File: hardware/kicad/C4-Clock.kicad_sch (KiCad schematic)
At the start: 39 parts, among them J1 Keypad, J2 Battery, J3 LCD1602, J4 Boost Module, J5 ICSP, K1 FINDER-36.11-5V, Q1 S9014, Q2 S9014, Q3 S9014, SW1 SW_SPST, SW2 SW_SPST, U1 ATmega328P-P, U2 AMS1117-5.0, U3 PCF8574A, U4 DS1302+, Y1 16MHz, Y2 32.768kHz

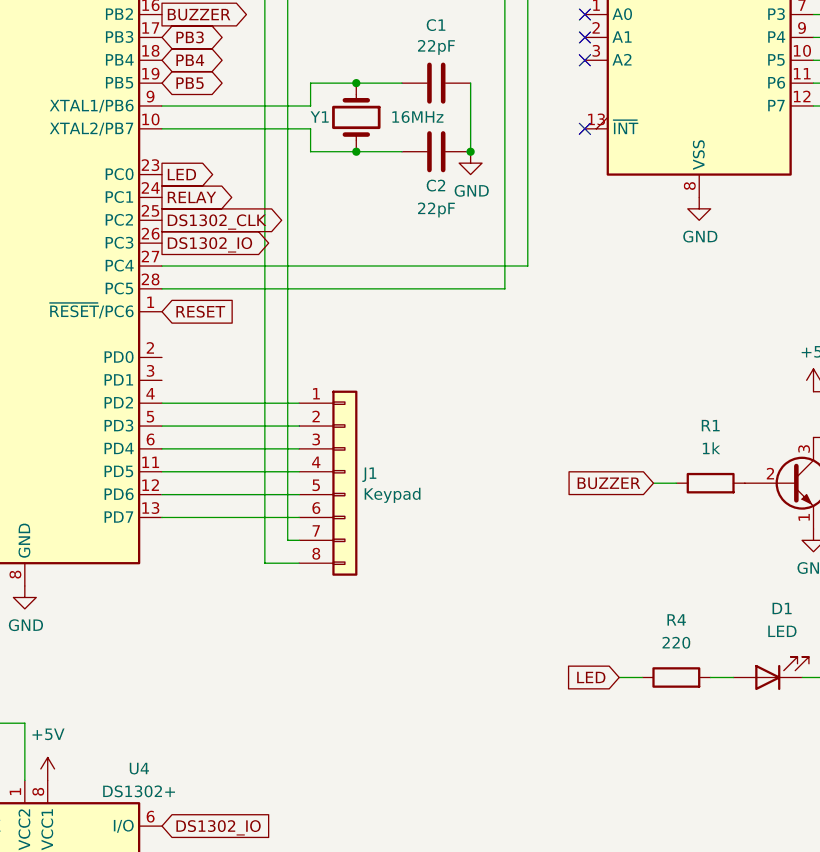
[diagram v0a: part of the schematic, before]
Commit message: kicad: Remove unused pin A0
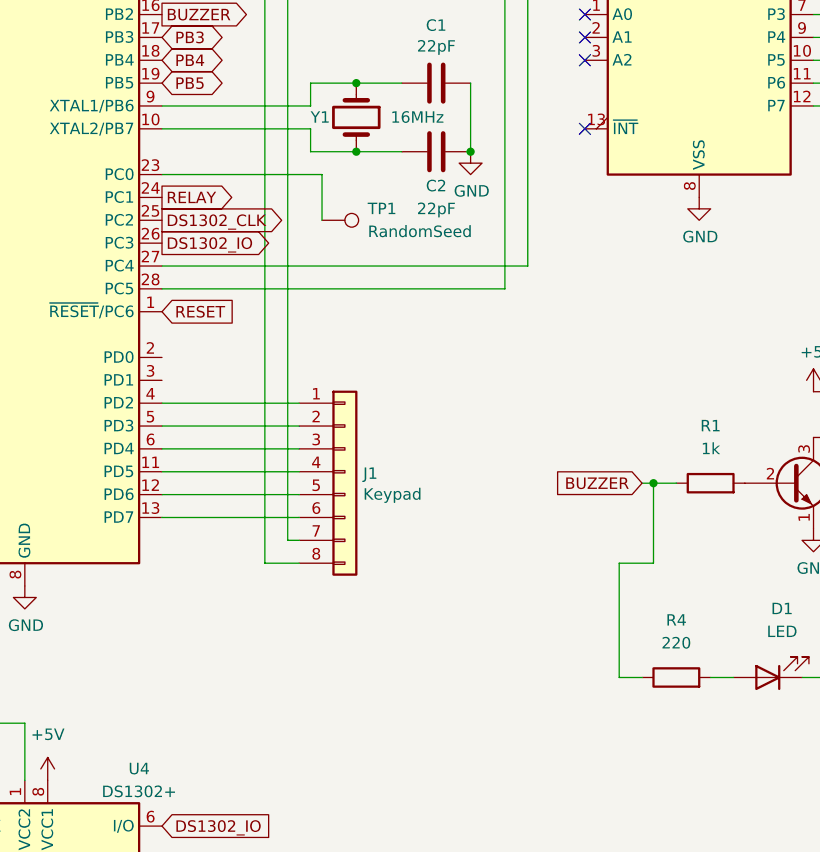
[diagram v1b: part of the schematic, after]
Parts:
- added TP1: RandomSeed, TestPoint:TestPoint_Pad_D1.0mm, symbol Connector:TestPoint
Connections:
- net BUZZER: now also R4.1
- net LED: no longer names the net of U1.23 (PC0)
- net LED: now also TP1.1; no longer R4.1
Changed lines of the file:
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@@
   (junction (at 228.6 67.31) (diameter 0) (color 0 0 0 0)
+  )
+  (junction (at 139.7 113.03) (diameter 0) (color 0 0 0 0)
   )
   (junction (at 119.38 76.2) (diameter 0) (color 0 0 0 0)
@@
     (stroke (width 0) (type default) (color 0 0 0 0))
   )
+  (wire (pts (xy 85.09 78.74) (xy 102.87 78.74))
+    (stroke (width 0) (type default) (color 0 0 0 0))
+  )
   (wire (pts (xy 106.68 68.58) (xy 111.76 68.58))
     (stroke (width 0) (type default) (color 0 0 0 0))
@@
     (stroke (width 0) (type default) (color 0 0 0 0))
   )
+  (wire (pts (xy 135.89 121.92) (xy 135.89 134.62))
+    (stroke (width 0) (type default) (color 0 0 0 0))
+  )
   (wire (pts (xy 220.98 135.89) (xy 213.36 135.89))
     (stroke (width 0) (type default) (color 0 0 0 0))
@@
     (stroke (width 0) (type default) (color 0 0 0 0))
   )
+  (wire (pts (xy 139.7 121.92) (xy 135.89 121.92))
+    (stroke (width 0) (type default) (color 0 0 0 0))
+  )
   (wire (pts (xy 71.12 44.45) (xy 69.85 44.45))
     (stroke (width 0) (type default) (color 0 0 0 0))
@@
     (stroke (width 0) (type default) (color 0 0 0 0))
   )
+  (wire (pts (xy 138.43 113.03) (xy 139.7 113.03))
+    (stroke (width 0) (type default) (color 0 0 0 0))
+  )
+  (wire (pts (xy 190.5 135.89) (xy 205.74 135.89))
+    (stroke (width 0) (type default) (color 0 0 0 0))
+  )
+  (wire (pts (xy 236.22 114.3) (xy 236.22 116.84))
+    (stroke (width 0) (type default) (color 0 0 0 0))
+  )
+  (wire (pts (xy 228.6 62.23) (xy 228.6 67.31))
+    (stroke (width 0) (type default) (color 0 0 0 0))
+  )
+  (wire (pts (xy 212.09 67.31) (xy 212.09 72.39))
+    (stroke (width 0) (type default) (color 0 0 0 0))
+  )
+  (wire (pts (xy 96.52 121.92) (xy 96.52 58.42))
+    (stroke (width 0) (type default) (color 0 0 0 0))
+  )
+  (wire (pts (xy 220.98 114.3) (xy 220.98 116.84))
+    (stroke (width 0) (type default) (color 0 0 0 0))
+  )
+  (wire (pts (xy 102.87 78.74) (xy 102.87 83.82))
+    (stroke (width 0) (type default) (color 0 0 0 0))
+  )
   (wire (pts (xy 139.7 113.03) (xy 142.24 113.03))
     (stroke (width 0) (type default) (color 0 0 0 0))
   )
-  (wire (pts (xy 190.5 135.89) (xy 205.74 135.89))
-    (stroke (width 0) (type default) (color 0 0 0 0))
-  )
-  (wire (pts (xy 236.22 114.3) (xy 236.22 116.84))
-    (stroke (width 0) (type default) (color 0 0 0 0))
-  )
-  (wire (pts (xy 228.6 62.23) (xy 228.6 67.31))
-    (stroke (width 0) (type default) (color 0 0 0 0))
-  )
-  (wire (pts (xy 212.09 67.31) (xy 212.09 72.39))
-    (stroke (width 0) (type default) (color 0 0 0 0))
-  )
-  (wire (pts (xy 96.52 121.92) (xy 96.52 58.42))
-    (stroke (width 0) (type default) (color 0 0 0 0))
-  )
-  (wire (pts (xy 220.98 114.3) (xy 220.98 116.84))
-    (stroke (width 0) (type default) (color 0 0 0 0))
-  )
   (wire (pts (xy 96.52 58.42) (xy 85.09 58.42))
     (stroke (width 0) (type default) (color 0 0 0 0))
@@
   )
   (wire (pts (xy 85.09 116.84) (xy 100.33 116.84))
+    (stroke (width 0) (type default) (color 0 0 0 0))
+  )
+  (wire (pts (xy 139.7 113.03) (xy 139.7 121.92))
     (stroke (width 0) (type default) (color 0 0 0 0))
   )
@@
   (text "En" (at 200.66 50.8 0)
     (effects (font (size 1.27 1.27)) (justify left bottom))
-  )
-  (global_label "LED" (shape input) (at 135.89 134.62 180) (fields_autoplaced)
-    (effects (font (size 1.27 1.27)) (justify right))
-    (property "Intersheet References" "${INTERSHEET_REFS}" (id 0) (at 130.1187 134.5406 0)
-      (effects (font (size 1.27 1.27)) (justify right) hide)
-    )
   )
   (global_label "PB5" (shape bidirectional) (at 30.48 34.29 180) (fields_autoplaced)
@@
     )
   )
-  (global_label "BUZZER" (shape input) (at 139.7 113.03 180) (fields_autoplaced)
+  (global_label "BUZZER" (shape input) (at 138.43 113.03 180) (fields_autoplaced)
     (effects (font (size 1.27 1.27)) (justify right))
-    (property "Intersheet References" "${INTERSHEET_REFS}" (id 0) (at -10.16 0 0)
+    (property "Intersheet References" "${INTERSHEET_REFS}" (id 0) (at -11.43 0 0)
       (effects (font (size 1.27 1.27)) hide)
     )
@@
     (property "Intersheet References" "${INTERSHEET_REFS}" (id 0) (at 22.4106 36.7506 0)
       (effects (font (size 1.27 1.27)) (justify right) hide)
-    )
-  )
-  (global_label "LED" (shape output) (at 85.09 78.74 0) (fields_autoplaced)
-    (effects (font (size 1.27 1.27)) (justify left))
-    (property "Intersheet References" "${INTERSHEET_REFS}" (id 0) (at 90.8613 78.6606 0)
-      (effects (font (size 1.27 1.27)) (justify left) hide)
     )
   )
@@
     (pin "2")
   )
+  (symbol (lib_id "Connector:TestPoint") (at 102.87 83.82 270) (unit 1)
+    (in_bom yes) (on_board yes) (fields_autoplaced)
+    (property "Reference" "TP1" (id 0) (at 107.95 82.5499 90)
+      (effects (font (size 1.27 1.27)) (justify left))
+    )
+    (property "Value" "RandomSeed" (id 1) (at 107.95 85.0899 90)
+      (effects (font (size 1.27 1.27)) (justify left))
+    )
+    (property "Footprint" "TestPoint:TestPoint_Pad_D1.0mm" (id 2) (at 102.87 88.9 0)
+      (effects (font (size 1.27 1.27)) hide)
+    )
+    (property "Datasheet" "~" (id 3) (at 102.87 88.9 0)
+      (effects (font (size 1.27 1.27)) hide)
+    )
+    (pin "1")
+  )
   (symbol (lib_id "Mechanical:MountingHole_Pad") (at 205.74 111.76 0) (unit 1)
     (in_bom yes) (on_board yes) (fields_autoplaced)
@@
       (reference "SW2") (unit 1) (value "SW_SPST") (footprint "Button_Switch_THT:SW_Push_2P2T_Toggle_CK_PVA2xxH1xxxxxxV2")
     )
+    (path "/49835dfc-d2d1-4b42-936d-27332303c393"
+      (reference "TP1") (unit 1) (value "RandomSeed") (footprint "TestPoint:TestPoint_Pad_D1.0mm")
+    )
     (path "/20f5379c-7d1a-4093-921b-363ef364bc02"

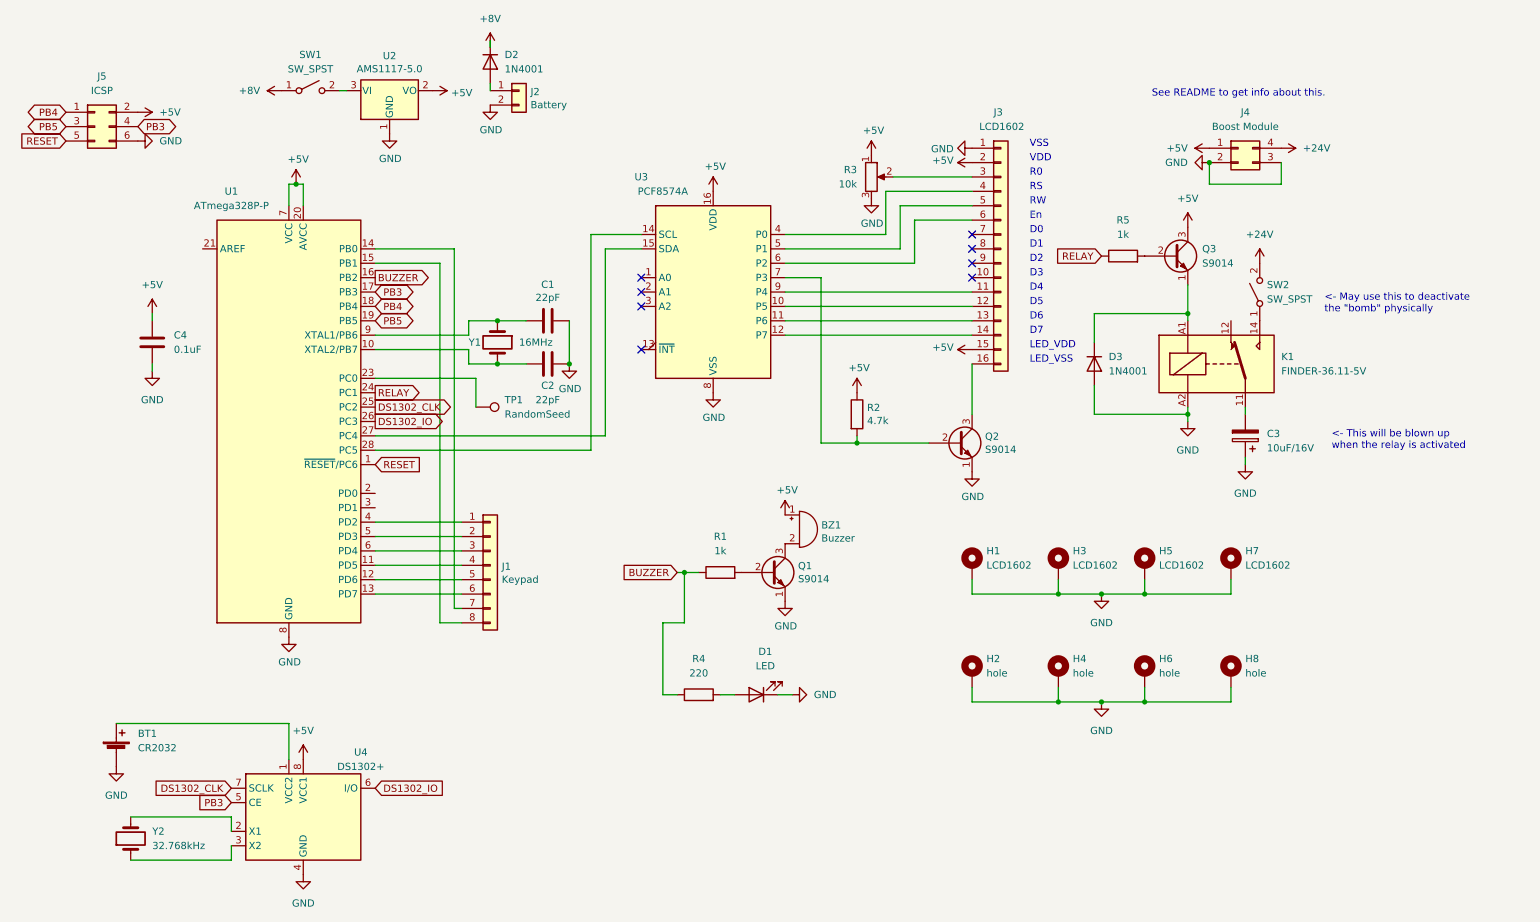
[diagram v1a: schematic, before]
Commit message: kicad: removed DS1302 and atmega
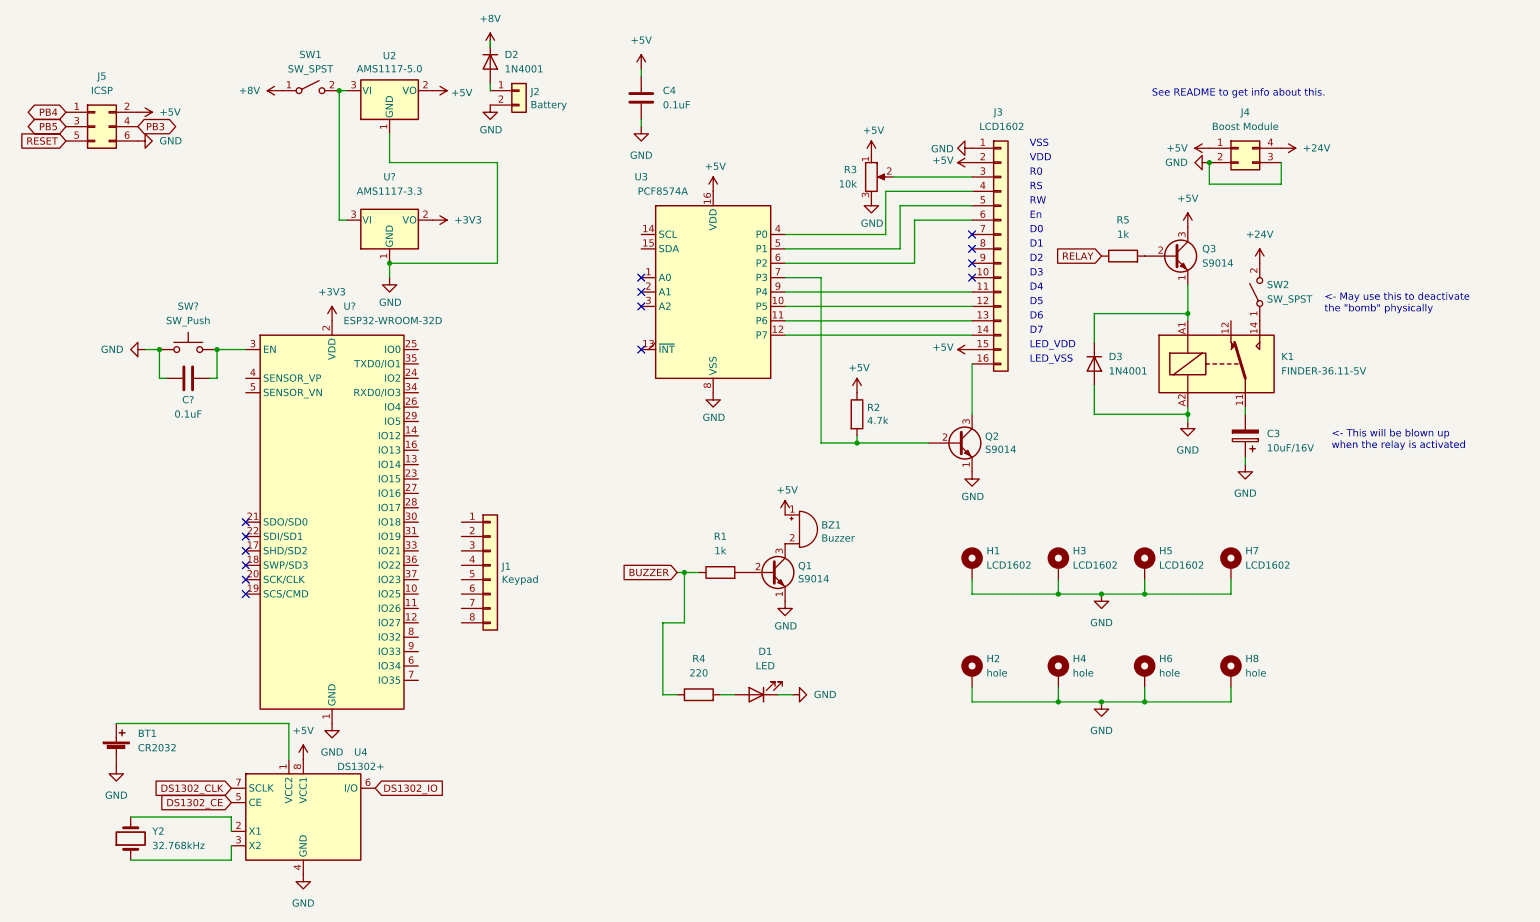
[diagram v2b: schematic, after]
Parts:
- removed C1, C2: 22pF, Capacitor_THT:C_Disc_D4.3mm_W1.9mm_P5.00mm, symbol Device:C
- removed TP1: RandomSeed, TestPoint:TestPoint_Pad_D1.0mm, symbol Connector:TestPoint
- removed U1: ATmega328P-P, Package_DIP:DIP-28_W7.62mm_Socket, symbol MCU_Microchip_ATmega:ATmega328P-P
- removed Y1: 16MHz, Crystal:Crystal_HC49-4H_Vertical, symbol Device:Crystal
- added C?: 0.1uF, symbol Device:C
- added SW?: SW_Push, symbol Switch:SW_Push
- added U?: AMS1117-3.3, Package_TO_SOT_SMD:SOT-223-3_TabPin2, symbol Regulator_Linear:AMS1117-3.3
- added U?: ESP32-WROOM-32D, RF_Module:ESP32-WROOM-32, symbol RF_Module:ESP32-WROOM-32D
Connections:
- net GND: now also C?.1, SW?.1, U?.1 (GND), U?.1 (GND), U?.15 (GND), U?.38 (GND), U?.39 (GND)
- net PB3: no longer U4.5 (CE)
- net at SW1.2 (B), U2.3 (VI): now also U?.3 (VI)
- new net: C?.2, SW?.2, U?.3 (EN)
- new net +3V3: U?.2 (VDD), U?.2 (VO)
- new net DS1302_CE: U4.5 (CE)
- no-connect marks 8 -> 14
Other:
- moved on the sheet: C4

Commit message: kicad: Change ATmega328P to ESP32-WROOM-32
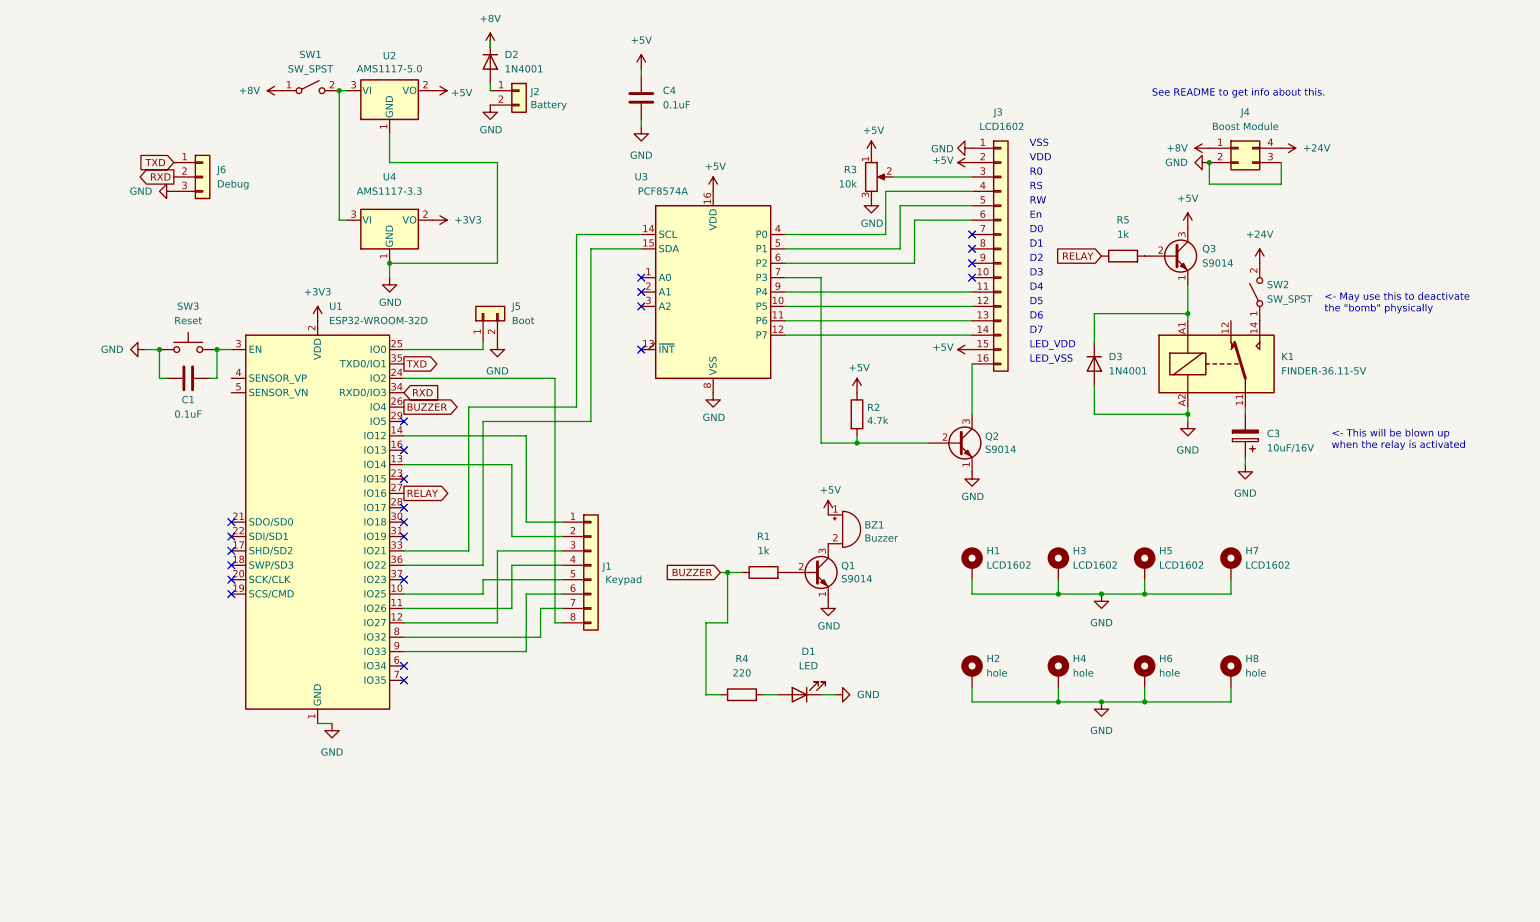
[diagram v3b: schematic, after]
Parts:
- removed BT1: CR2032, Battery:BatteryHolder_ComfortableElectronic_CH273-2450_1x2450, symbol Device:Battery_Cell
- removed J5: ICSP, Connector_PinHeader_2.54mm:PinHeader_2x03_P2.54mm_Vertical, symbol Connector_Generic:Conn_02x03_Odd_Even
- removed U4: DS1302+, Package_DIP:DIP-8_W7.62mm_Socket, symbol Timer_RTC:DS1302+
- removed Y2: 32.768kHz, Crystal:Crystal_AT310_D3.0mm_L10.0mm_Horizontal, symbol Device:Crystal
- added J5: Boot, Connector_PinHeader_2.54mm:PinHeader_1x02_P2.54mm_Vertical, symbol Connector_Generic:Conn_01x02
- added J6: Debug, Connector_PinHeader_2.54mm:PinHeader_1x03_P2.54mm_Vertical, symbol Connector_Generic:Conn_01x03
- C1: renamed from C?; footprint (none) -> Capacitor_THT:C_Disc_D4.3mm_W1.9mm_P5.00mm
- SW3: renamed from SW?; value SW_Push -> Reset; footprint (none) -> Button_Switch_THT:SW_PUSH_6mm_H5mm
- gave numbers to parts that had none: 2
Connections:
- net +5V: no longer J4.1 (Pin_1)
- net +8V: now also J4.1 (Pin_1)
- net BUZZER: now also U1.26 (IO4)
- net GND: now also J5.2 (Pin_2), J6.3 (Pin_3)
- net RELAY: now also U1.27 (IO16)
- net at U3.14 (SCL): now also U1.33 (IO21)
- net at U3.15 (SDA): now also U1.36 (IO22)
- net at J1.1 (Pin_1): now also U1.14 (IO12)
- net at J1.2 (Pin_2): now also U1.13 (IO14)
- net at J1.3 (Pin_3): now also U1.12 (IO27)
- net at J1.4 (Pin_4): now also U1.11 (IO26)
- net at J1.5 (Pin_5): now also U1.10 (IO25)
- net at J1.6 (Pin_6): now also U1.9 (IO33)
- net at J1.7 (Pin_7): now also U1.8 (IO32)
- net at J1.8 (Pin_8): now also U1.24 (IO2)
- net at U1.25 (IO0): now also J5.1 (Pin_1)
- net RXD: now reaches U1.34 (RXD0/IO3)
- net RXD: now also J6.2 (Pin_2)
- net TXD: now reaches U1.35 (TXD0/IO1)
- net TXD: now also J6.1 (Pin_1)
- no-connect marks 14 -> 23
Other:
- moved on the sheet: BZ1, D1, J1, Q1, R1, R4, U1
